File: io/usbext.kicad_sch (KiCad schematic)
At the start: 13 parts, among them J15 USB_A_Stacked

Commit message: External I/O
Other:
- moved on the sheet: C393, C395, C397, C399, C400, C401, D15, D16, D17, D18, F1, F2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

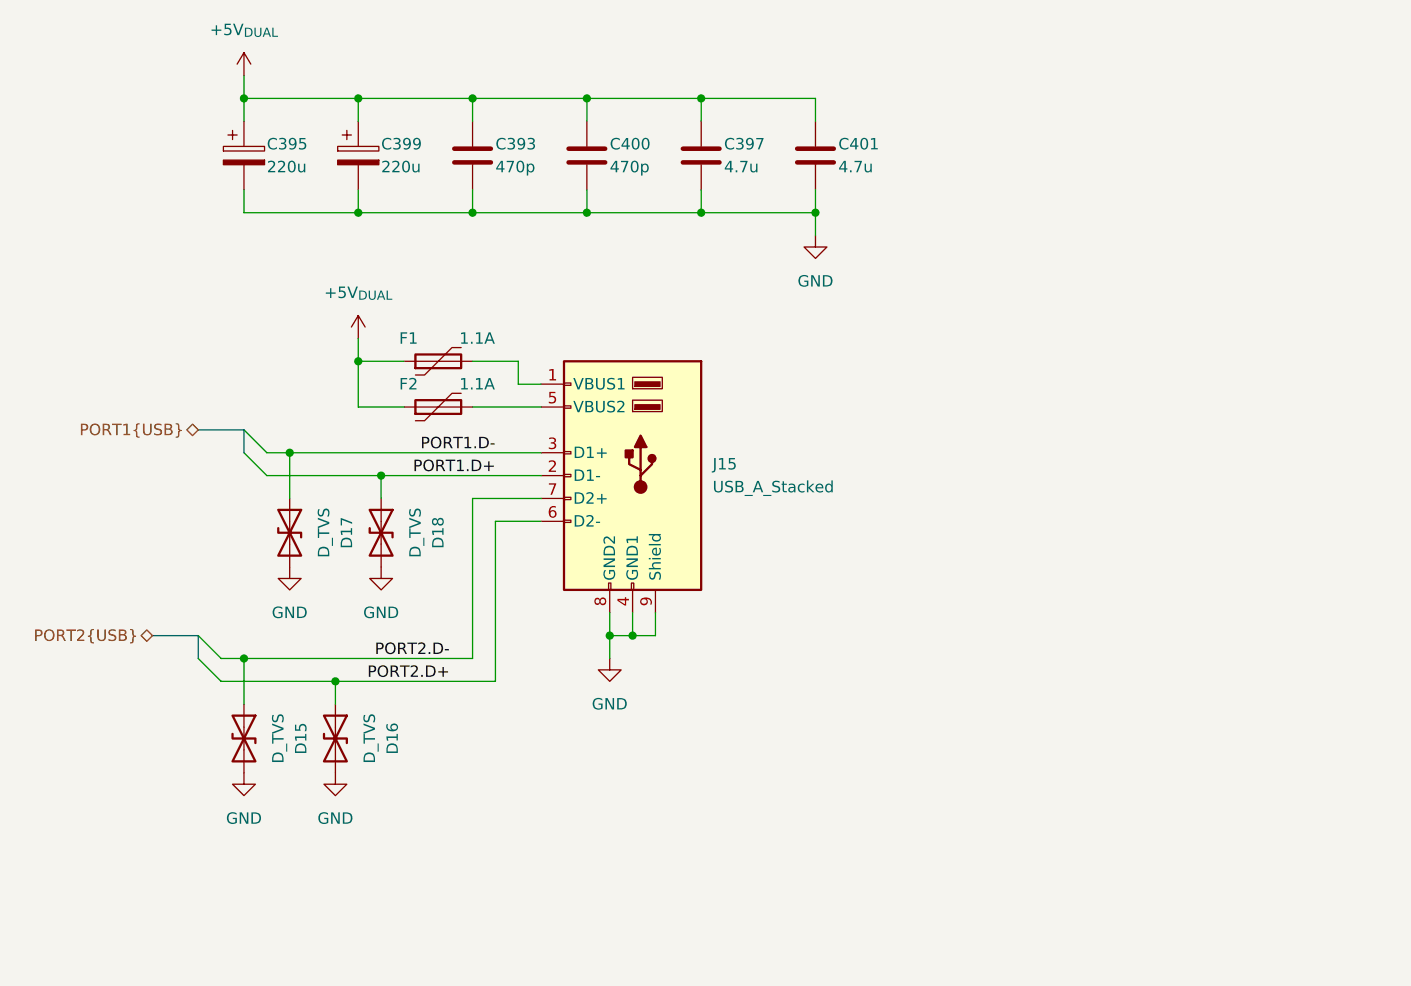
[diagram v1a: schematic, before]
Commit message: Multipurpose and standby power rails, Reannotated schematic
Added V_1P2, V_1P8, V_5P0DUAL, V_EFUSE, V_GPUPCIE, V_3P3STBY and V_1P2STBY
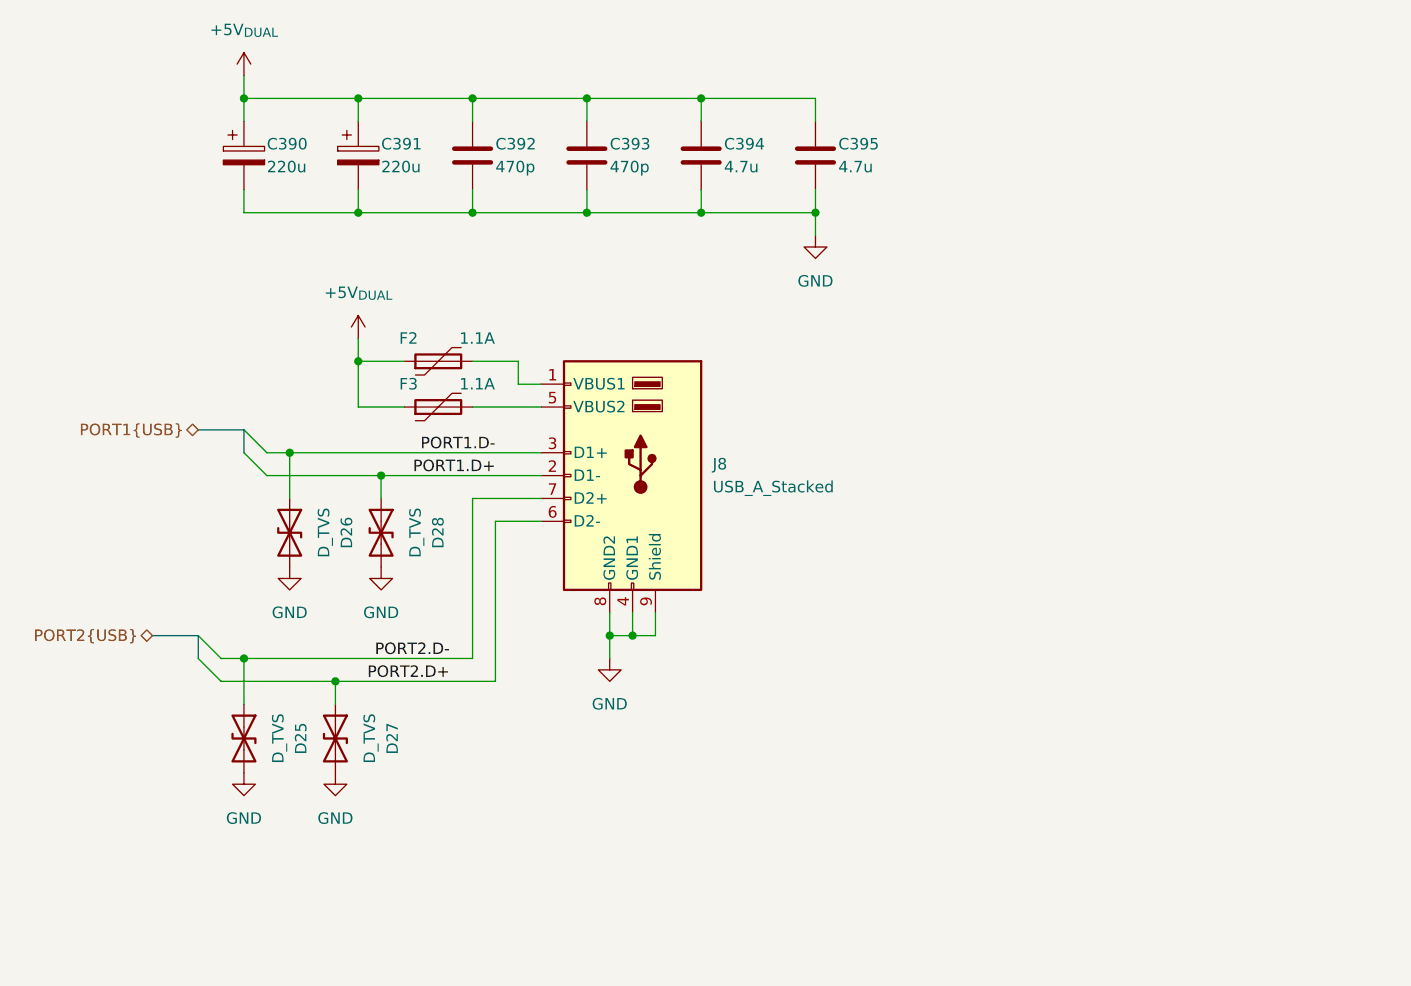
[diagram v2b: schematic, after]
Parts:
- renumbered C395 to C390, C399 to C391, C393 to C392, C400 to C393, C397 to C394, C401 to C395, D15 to D25, D17 to D26, D16 to D27, D18 to D28, F1 to F2, F2 to F3, J15 to J8
